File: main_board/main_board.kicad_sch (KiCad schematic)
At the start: 13 parts, among them J1 CON-SMA-EDGE-S, U2 TS5A4624DCKR, U4 TS5A4624DCKR

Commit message: update todos
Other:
- note added: "TODO: add headers for power and ground: +9V +5V GND"
- note added: "This voltage divider is intended to keep the signal within +5V to GND. Biasing only here should be fine, as the on resistance of each mux is very close to being a short circuit."
- note removed: "TODO: This voltage divider is intended to keep the signal within +5V to GND, but this approach need to be verified. (may have to bias on both sides of MUX)"
- note removed: "TODO: calculate coupling capacitor values"
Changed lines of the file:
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@@
 		)
 	)
-	(text "TODO: This voltage divider is intended to keep the signal within\n +5V to GND, but this approach need to be verified. (may have to \nbias on both sides of MUX)"
+	(text "TODO: add headers for power and ground: \n+9V \n+5V \nGND"
 		(exclude_from_sim no)
-		(at 70.358 103.378 0)
+		(at 114.808 118.364 0)
 		(effects
 			(font
@@
 		)
 	)
-	(text "TODO: calculate coupling capacitor values"
+	(text "This voltage divider is intended to keep the signal within\n+5V to GND. Biasing only here should be fine, as the on resistance \nof each mux is very close to being a short circuit."
 		(exclude_from_sim no)
-		(at 132.334 99.314 0)
+		(at 70.358 103.378 0)
 		(effects
 			(font

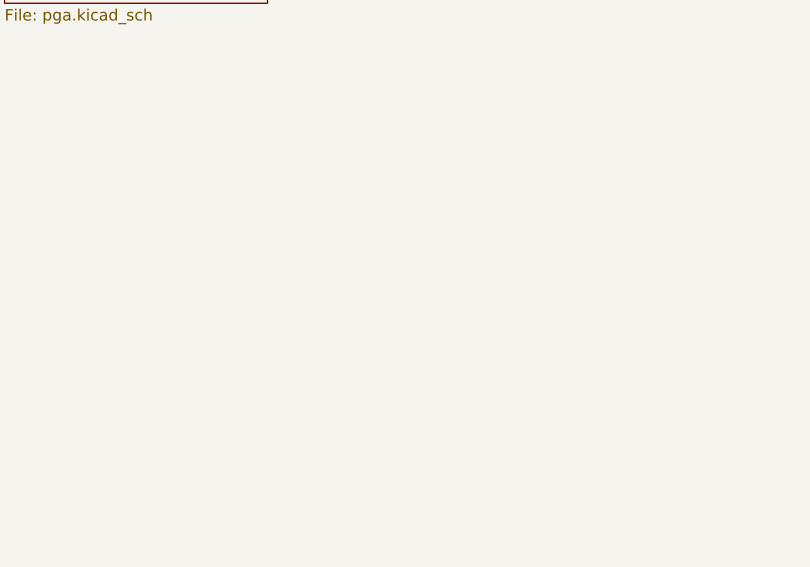
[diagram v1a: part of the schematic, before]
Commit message: added power headers.
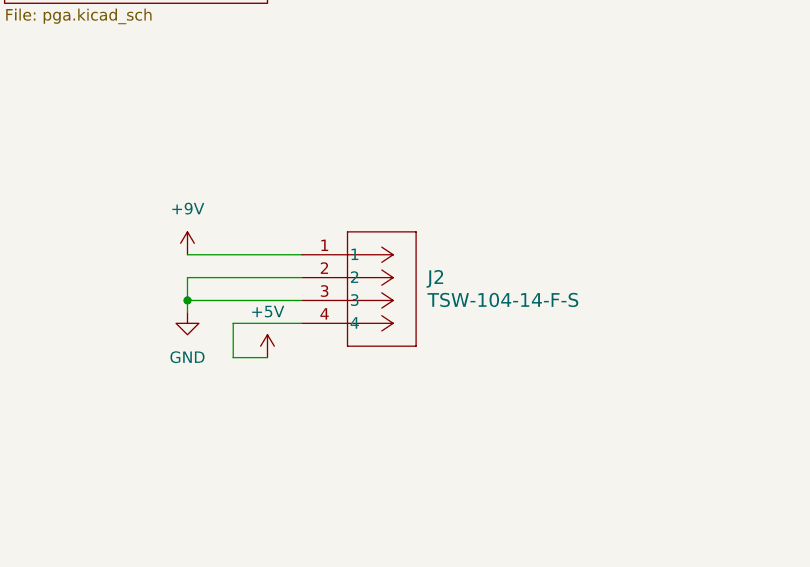
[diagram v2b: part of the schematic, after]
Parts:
- added J2: TSW-104-14-F-S, pin_header_fp:CON4_1X4_TU_TSW, symbol pin_header:TSW-104-14-F-S
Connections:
- net +5V: now also J2.4
- net GND: now also J2.2, J2.3
- new net +9V: J2.1

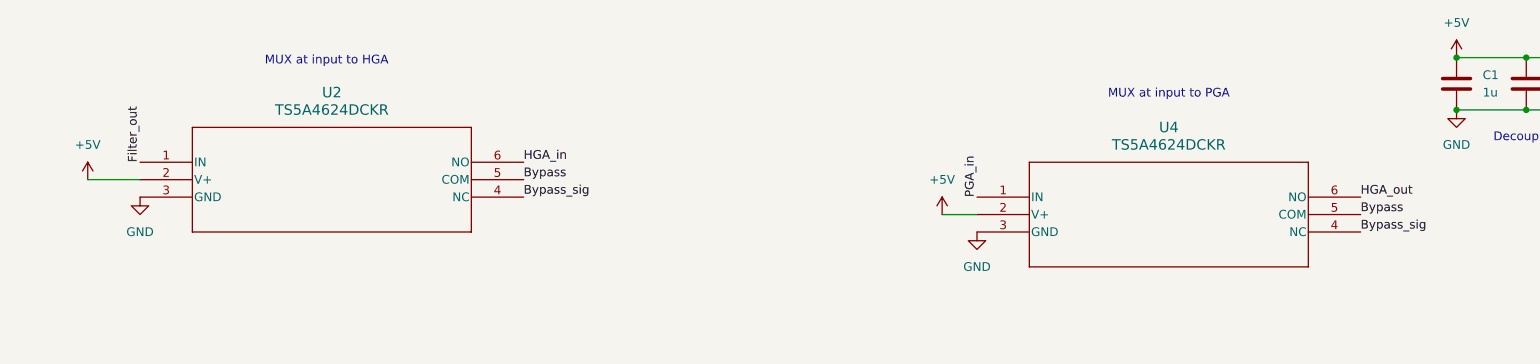
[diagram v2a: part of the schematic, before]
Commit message: fix signal connections to muxes
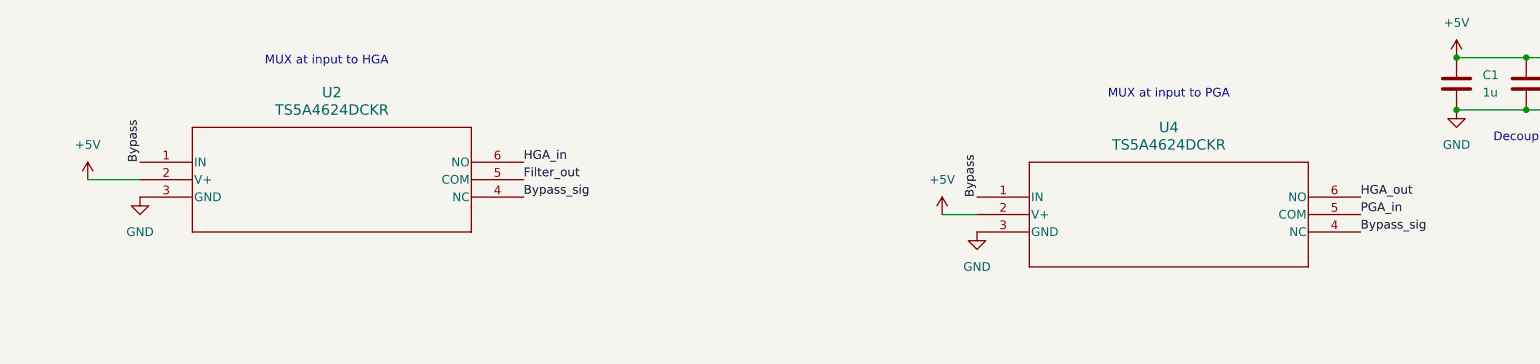
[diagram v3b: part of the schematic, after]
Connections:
- net Bypass: now also U2.1 (IN), U4.1 (IN); no longer U2.5 (COM), U4.5 (COM)
- net Filter_out: now also U2.5 (COM); no longer U2.1 (IN)
- net PGA_in: now also U4.5 (COM); no longer U4.1 (IN)
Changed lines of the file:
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@@
 	)
 	(label "Bypass"
-		(at 111.76 36.83 0)
+		(at 55.88 34.29 90)
 		(effects
 			(font
@@
 	)
 	(label "Filter_out"
-		(at 55.88 34.29 90)
+		(at 111.76 36.83 0)
 		(effects
 			(font
@@
 	)
 	(label "PGA_in"
-		(at 177.8 39.37 90)
+		(at 233.68 41.91 0)
 		(effects
 			(font
@@
 	)
 	(label "Bypass"
-		(at 233.68 41.91 0)
+		(at 177.8 39.37 90)
 		(effects
 			(font

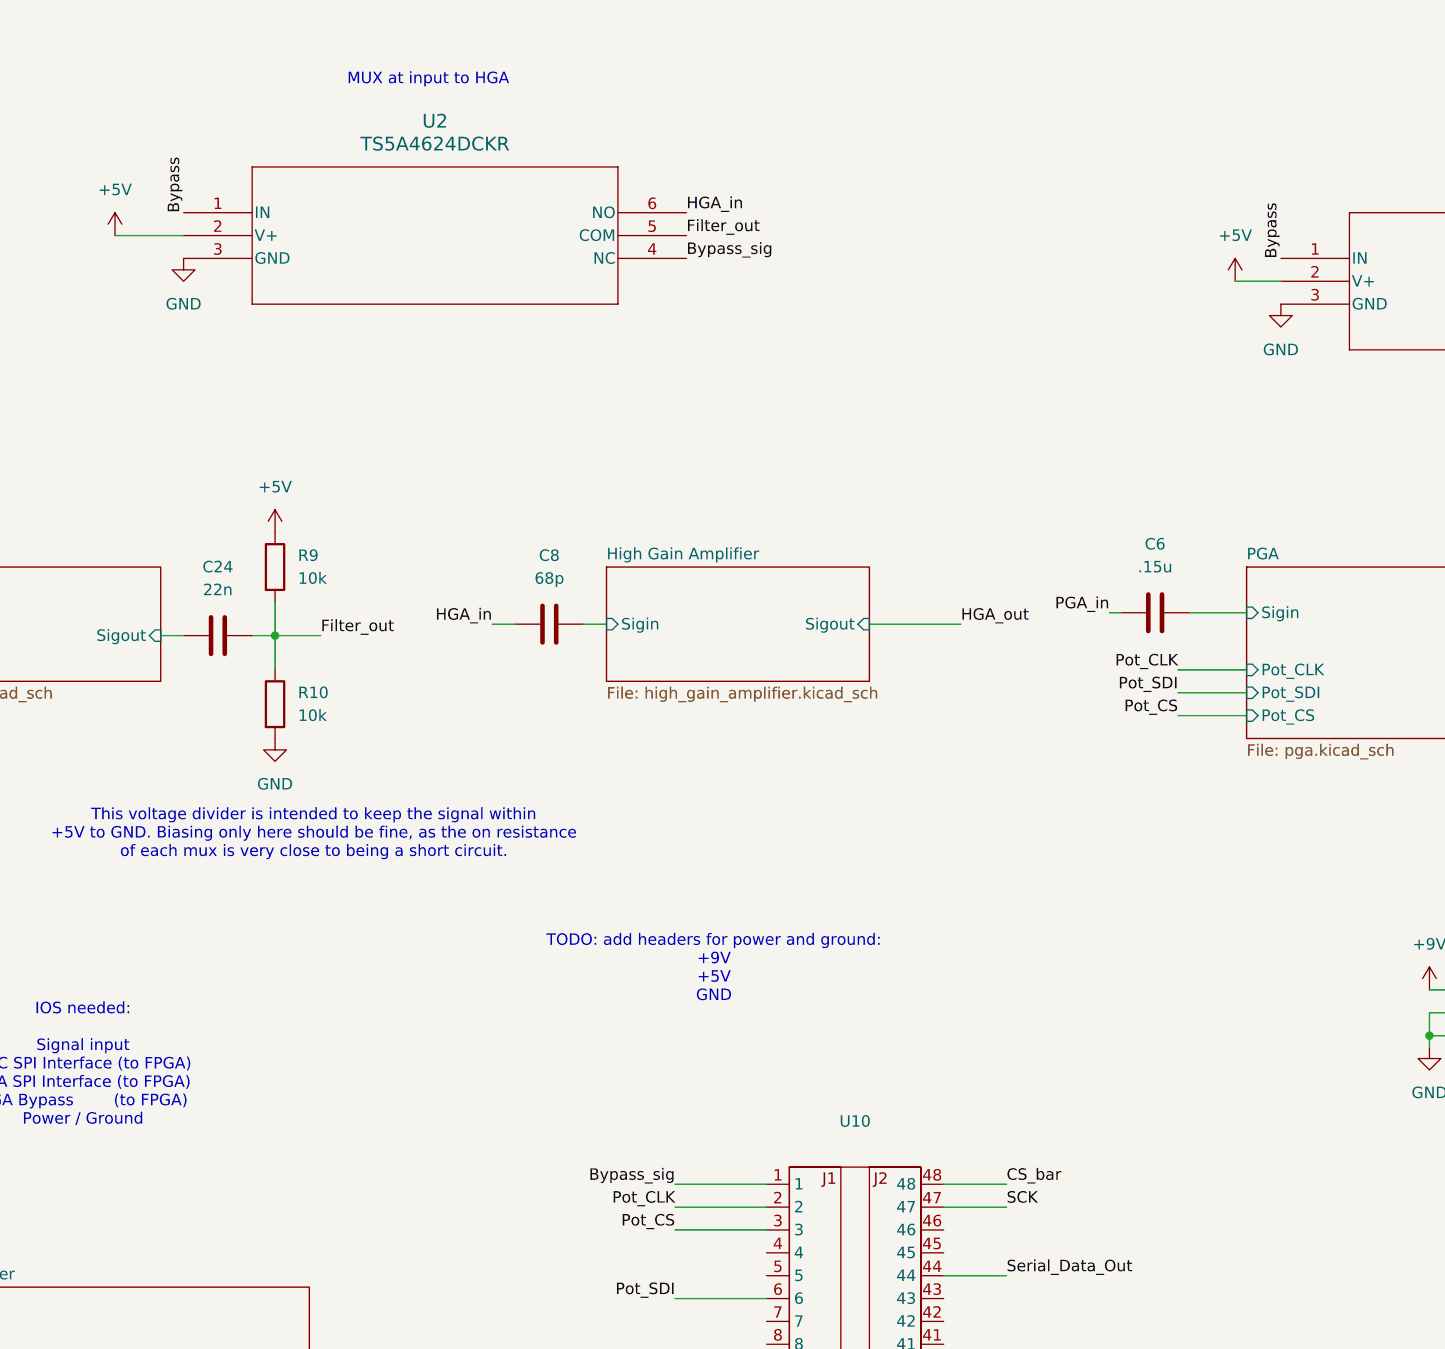
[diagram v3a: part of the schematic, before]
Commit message: fix control signal for hga bypass
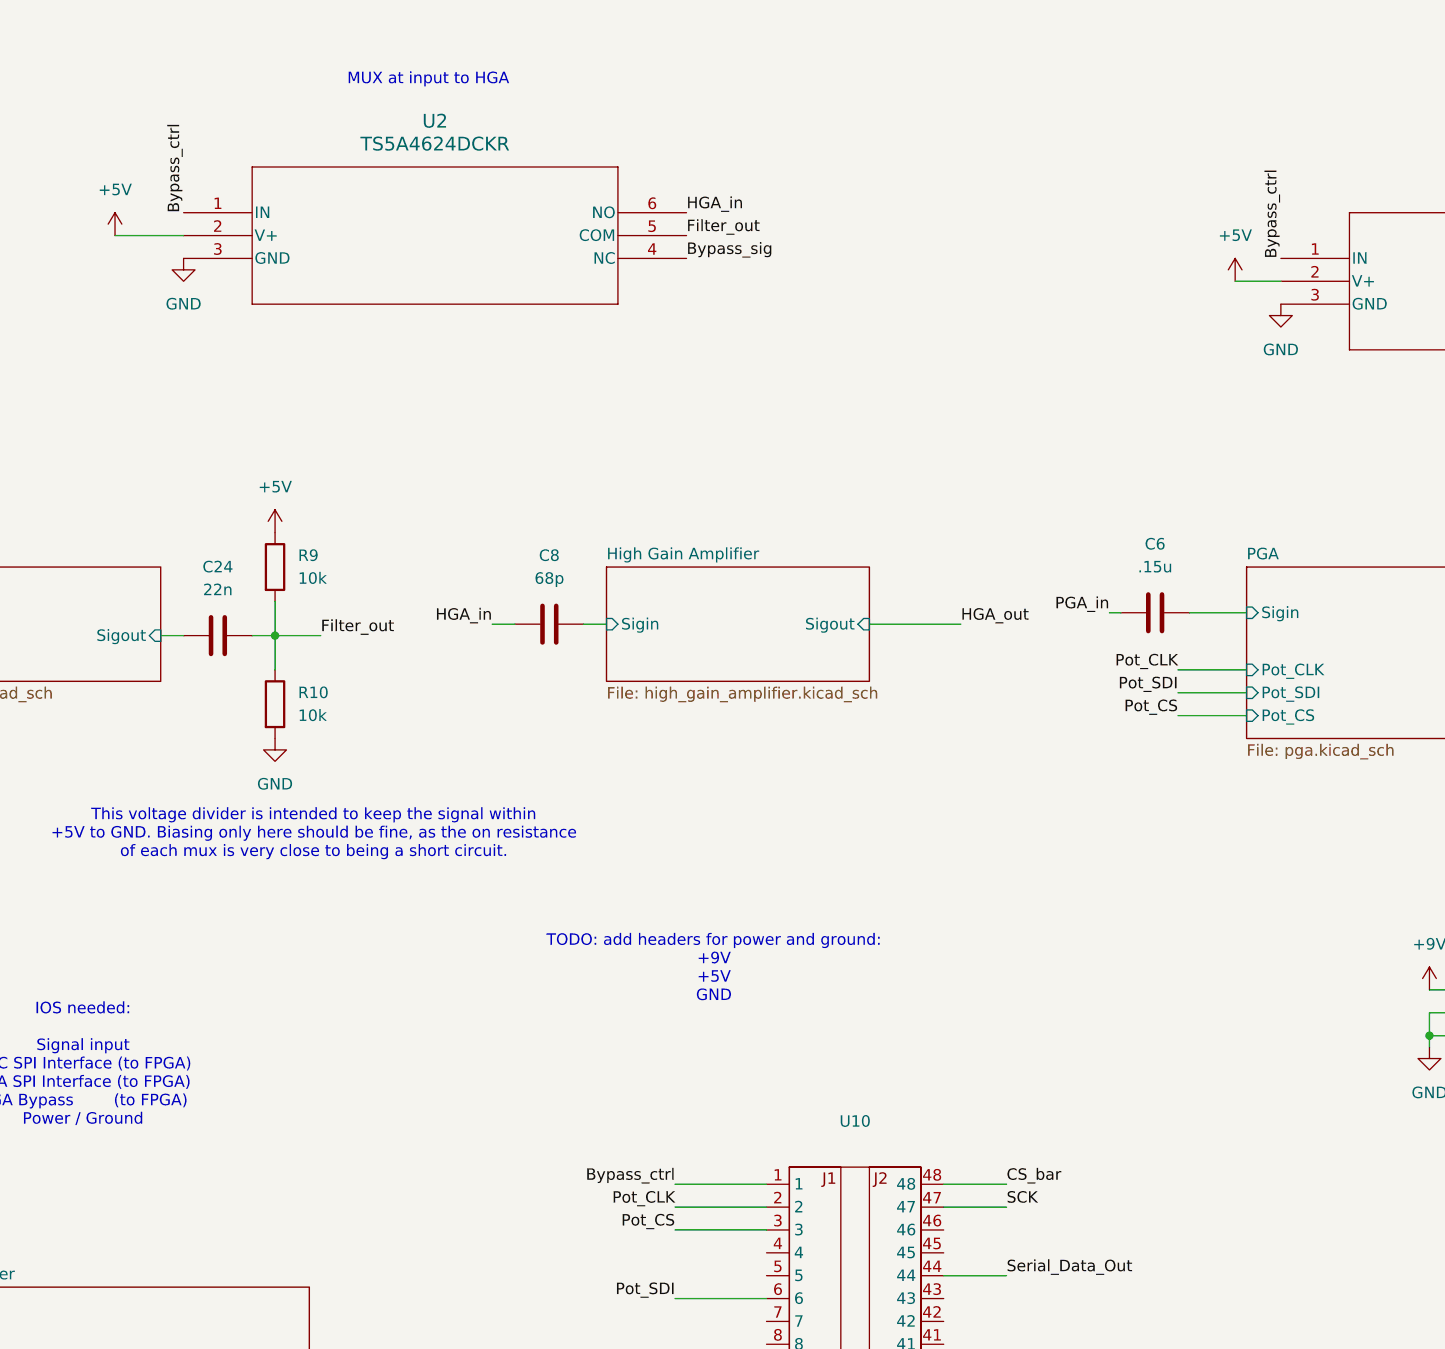
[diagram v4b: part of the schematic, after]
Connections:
- net Bypass_sig: no longer U10.1
- net Bypass renamed Bypass_ctrl
- net Bypass_ctrl: now also U10.1
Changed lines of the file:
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@@
 		)
 	)
-	(label "Bypass"
+	(label "Bypass_ctrl"
 		(at 55.88 34.29 90)
 		(effects
@@
 		)
 	)
-	(label "Bypass_sig"
+	(label "Bypass_ctrl"
 		(at 110.49 142.24 180)
 		(effects
@@
 		)
 	)
-	(label "Bypass"
+	(label "Bypass_ctrl"
 		(at 177.8 39.37 90)
 		(effects

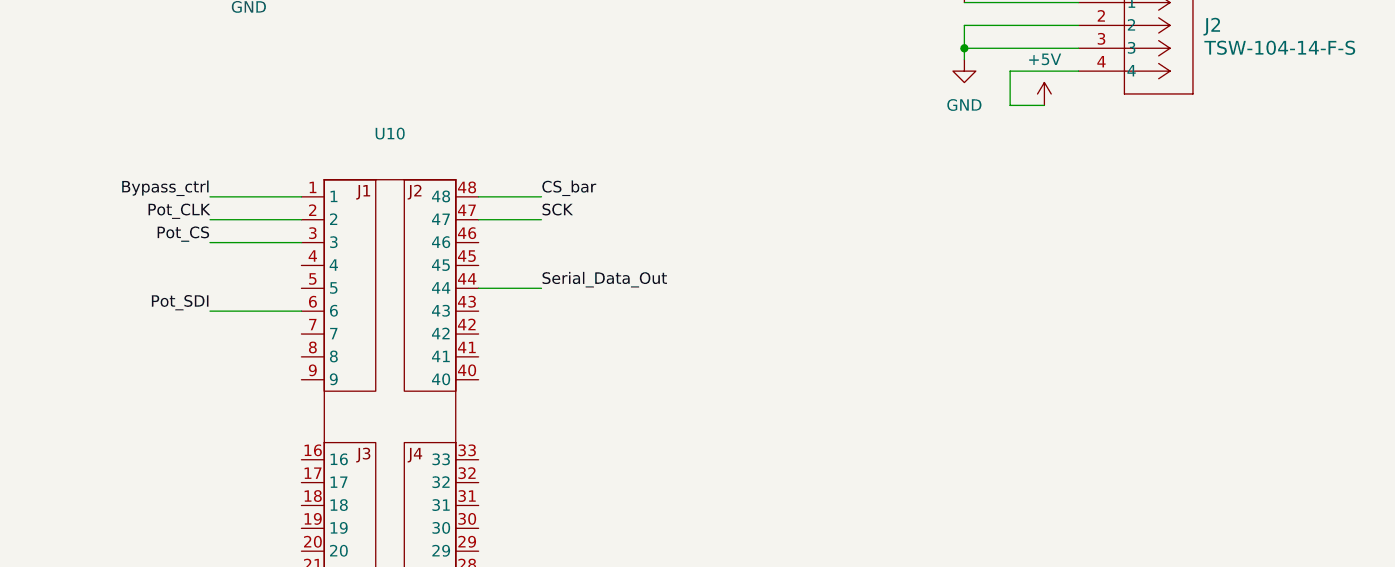
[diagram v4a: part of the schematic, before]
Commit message: added pin for uart.
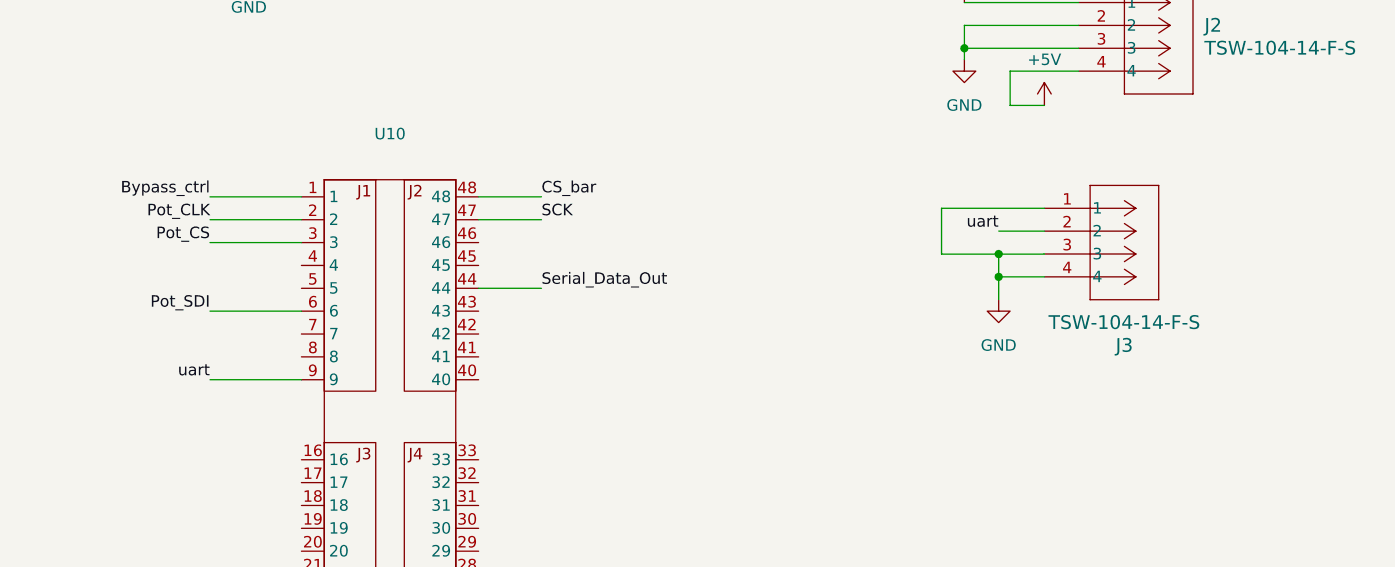
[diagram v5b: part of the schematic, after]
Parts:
- added J3: TSW-104-14-F-S, pin_header_fp:CON4_1X4_TU_TSW, symbol pin_header:TSW-104-14-F-S
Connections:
- net GND: now also J3.1, J3.3, J3.4
- net uart: now reaches U10.9
- net uart: now also J3.2
